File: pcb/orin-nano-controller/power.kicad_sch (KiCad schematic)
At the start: 4 parts, among them U3 ADP1715ARMZ-3.3-R7

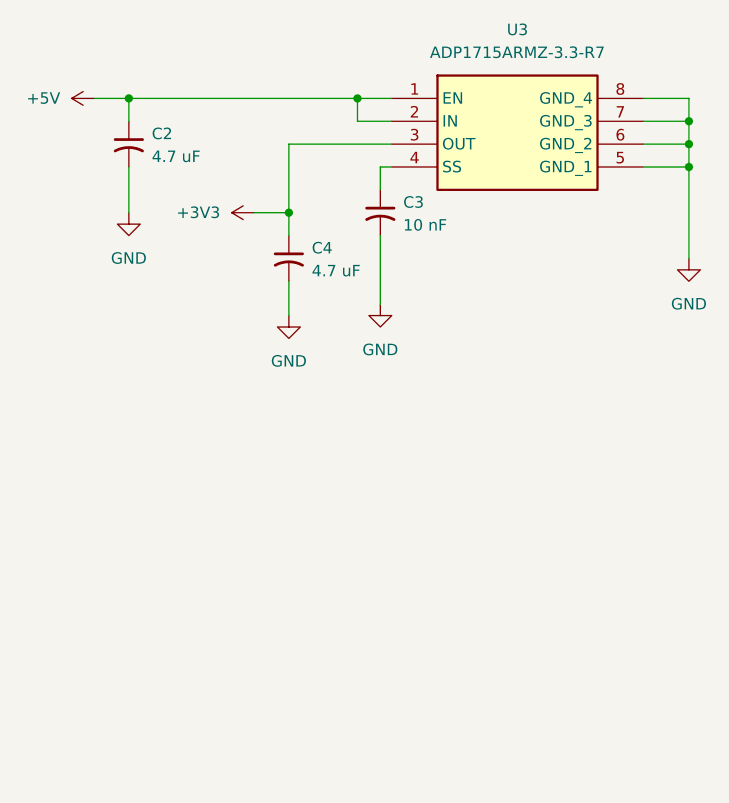
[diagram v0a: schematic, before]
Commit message: replace ldo
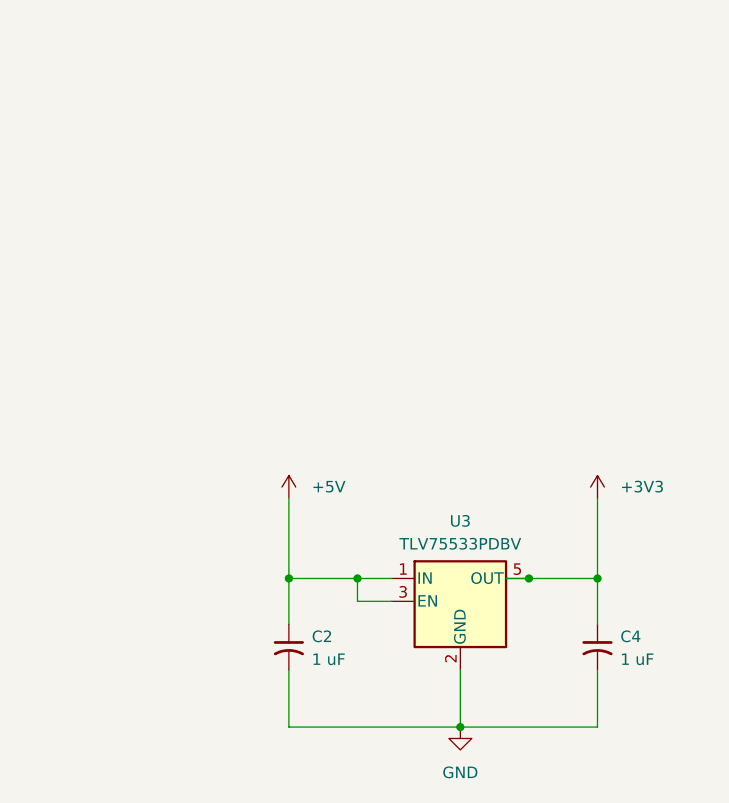
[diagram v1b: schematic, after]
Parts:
- removed C3: 10 nF, Capacitor_SMD:C_0805_2012Metric_Pad1.18x1.45mm_HandSolder, symbol Device:C_Small_US
- removed U3: ADP1715ARMZ-3.3-R7, SamacSys:SOP65P490X110-8N, symbol SamacSys:ADP1715ARMZ-3.3-R7
- added U3: TLV75533PDBV, Package_TO_SOT_SMD:SOT-23-5, symbol Regulator_Linear:TLV75533PDBV
- C2, C4: value 4.7 uF -> 1 uF
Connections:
- net +3V3: now also U3.5 (OUT)
- net +5V: now also U3.1 (IN), U3.3 (EN)
- net GND: now also U3.2 (GND)
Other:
- moved on the sheet: C2, C4
